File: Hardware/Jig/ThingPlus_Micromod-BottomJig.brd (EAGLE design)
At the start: 124.5 x 97.8 mm, 116 parts, among them J4 USB_A_PTH_MALE, J5 USB_A_SMT_FEMALE, U2 74LVC4066, U3 74LVC4066, U5 74LVC4066_MUX_1:1_X4

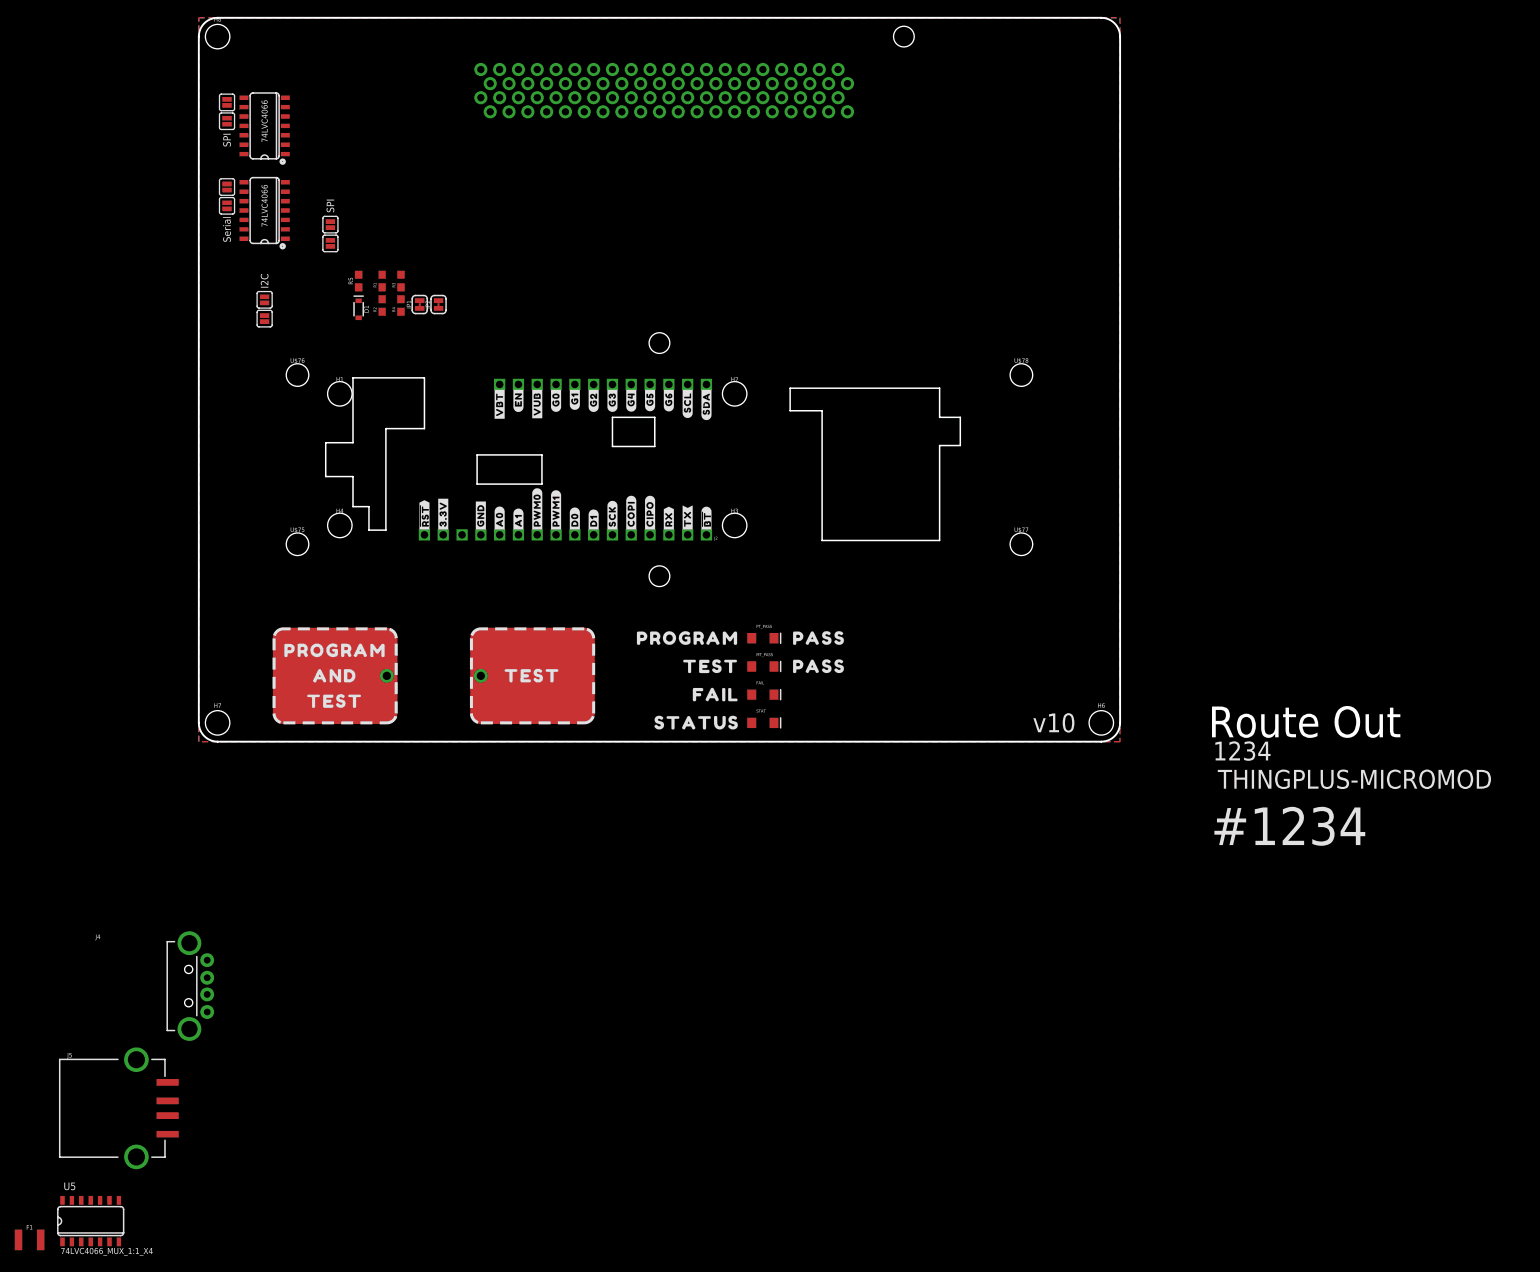
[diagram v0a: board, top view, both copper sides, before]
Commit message: Preliminary version of test jig bottom board uploaded
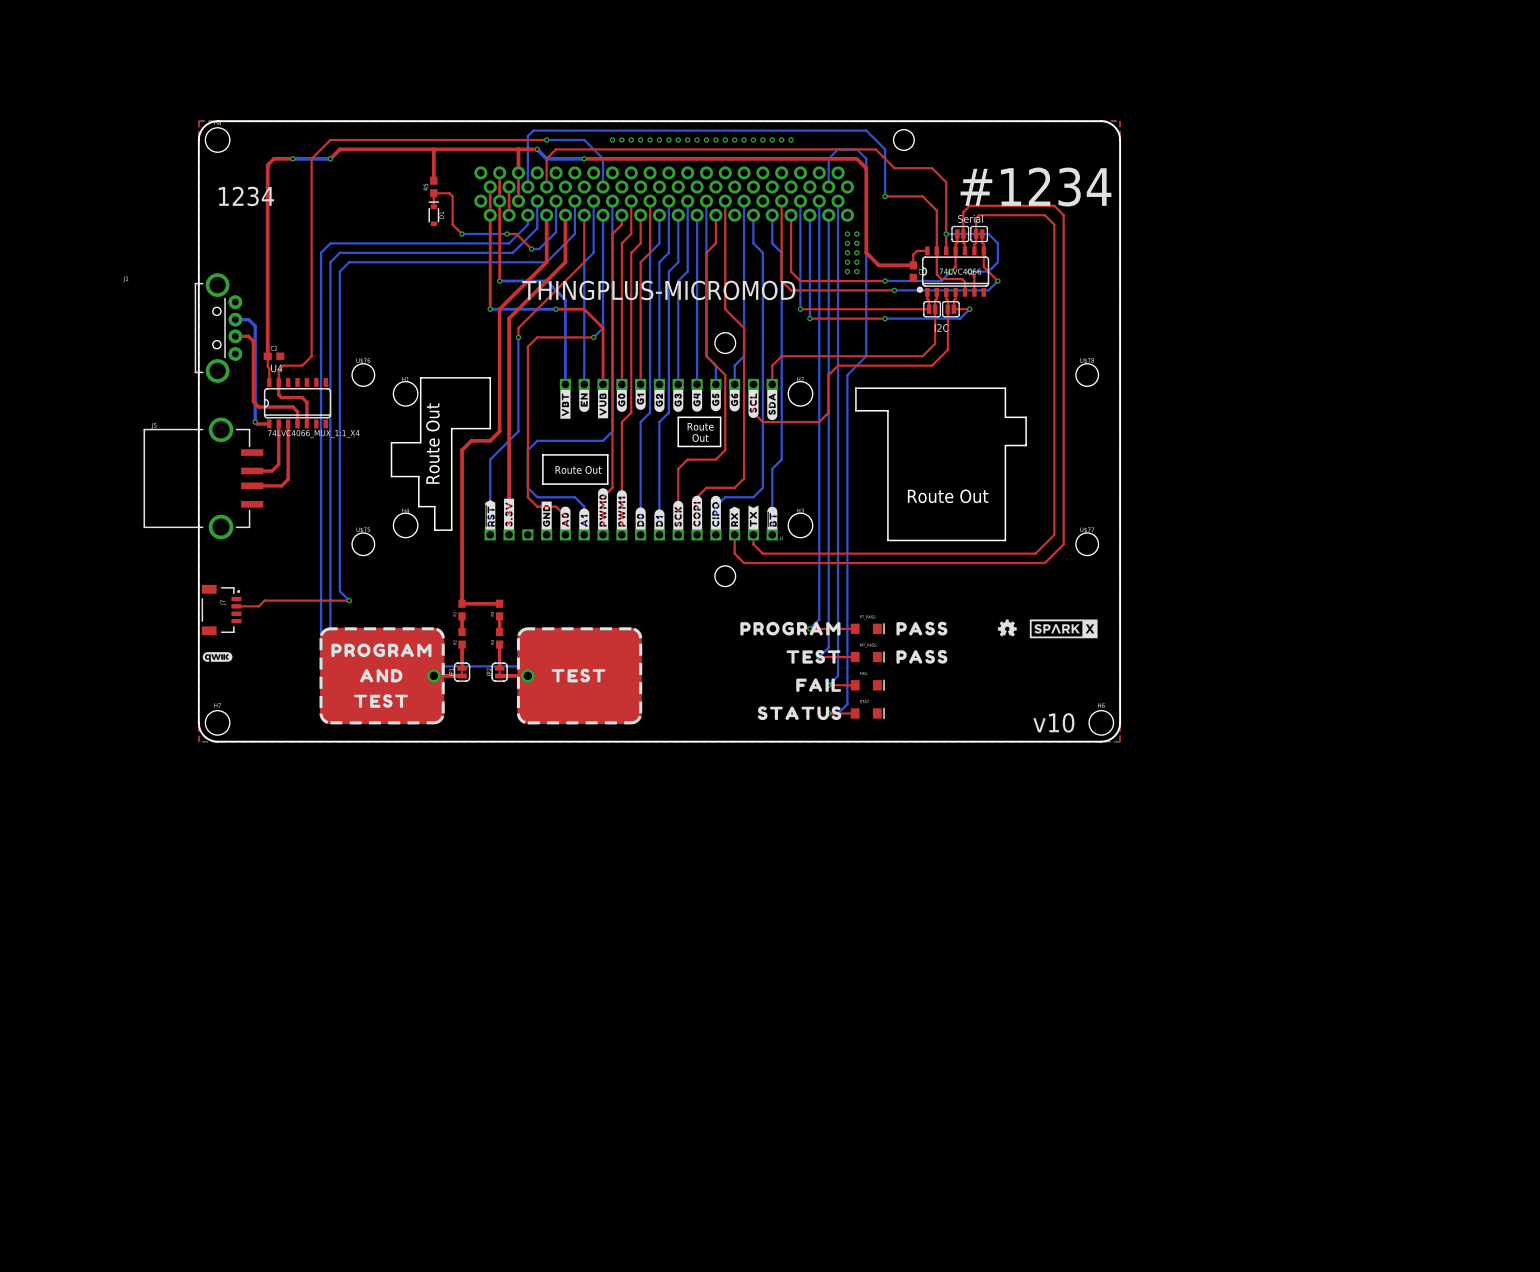
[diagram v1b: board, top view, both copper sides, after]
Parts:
- removed F1: 6V/2A, SparkFun-Fuses:1210
- removed J4: USB_A_PTH_MALE, SparkFun-Connectors:USB-A-H
- removed J_SCL3, J_SCL4, J_SCL5, J_SDA1: JUMPER-SMT_2_NO_SILK, SparkFun-Jumpers:SMT-JUMPER_2_NO_SILK
- removed U$41: (no value), output:#VE#16
- removed U$66: (no value), output:#MEAS#25
- removed U$69: (no value), output:#3#3V_LED#25
- removed U$70: (no value), output:#VIN_LED#25
- removed U$72: (no value), output:#I2C#27
- removed U$73: (no value), output:THINGPLUS_MICROMOD29
- removed U$74: (no value), output:#SCL#G7#27
- removed U$81: TB_MAIN_BRAIN_CARDEDGE_TB_SIDE, Testing:TB_CARDEDGE
- removed U3: 74LVC4066, SparkFun-IC-Logic:SO14
- removed U5: 74LVC4066_MUX_1:1_X4, Testing:SO14
- added C1, C2: 0.1uF, SparkFun-Capacitors:0603
- added J1: USB_A_PTH_MALE, SparkFun-Connectors:USB-A-H
- added J7: QWIIC_RIGHT_ANGLE, SparkFun-Connectors:JST04_1MM_RA
- added LOGO2: OSHW-LOGOMINI, SparkFun-Aesthetics:OSHW-LOGO-MINI
- added LOGO4: QWIIC_LOGO_4MM, SparkFun-Aesthetics:QWIIC_4MM
- added U$1: SPARKX-LOGO4, SparkX:SPARKX-MEDIUM
- added U1: TB_MAIN_BRAIN_CARDEDGE_TB_SIDE, Testing:TB_CARDEDGE
- added U4: 74LVC4066_MUX_1:1_X4, Testing:SO14
- moved J_SCL1 101.8 mm to (114.3, 74.9), turned to 180 degrees
- moved J_SDA 99.1 mm to (111.8, 74.9), turned to 0 degrees
- moved U2 93.0 mm to (110.5, 69.8), turned to 0 degrees
- moved J_SCL 92.7 mm to (110.5, 64.8), turned to 180 degrees
- moved J_SCL2 90.2 mm to (108.0, 64.8), turned to 0 degrees
- moved J5 85.9 mm to (8.89, 41.9)
- moved JP2 50.3 mm to (49.5, 15.7)
- moved JP1 50.0 mm to (44.5, 15.7)
- moved R4 46.9 mm to (49.5, 20.3)
- moved R3 46.4 mm to (49.5, 24.1)
- moved R2 46.2 mm to (44.5, 20.3)
- moved R1 45.7 mm to (44.5, 24.1)
- moved FRAME2 44.1 mm to (53.3, -8.89)
- moved D1 16.3 mm to (40.6, 77.5)
- moved R5 16.3 mm to (40.6, 81.3)
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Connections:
- removed net !BOOT!: J2.1
- removed net !RST!: J2.16
- removed net 3.3V: J2.15
- removed net A0: J2.12
- removed net A1: J2.11
- removed net D0: J2.8
- removed net D1: J2.7
- removed net EN: J3.11
- removed net G0: J3.9
- removed net G1: J3.8
- removed net G2: J3.7
- removed net G3: J3.6
- removed net G4: J3.5
- removed net G5: J3.4
- removed net G6: J3.3
- removed net J_10: U$81.P38
- removed net J_11: U$81.P34
- removed net J_12: U$81.P30
- removed net J_13: U$81.P26
- removed net J_14: U$81.P23
- removed net J_15: U$81.P21
- removed net J_16: U$81.P19
- removed net J_17: U$81.P17
- removed net J_2: U$81.P37
- removed net J_27: U$81.P50
- removed net J_28: U$81.P46
- removed net J_29: U$81.P42
- removed net J_3: U$81.P35
- removed net J_5: U$81.P33
- removed net J_6: U$81.P31
- removed net J_7: U$81.P29
- removed net J_8: U$81.P27
- removed net J_9: U$81.P25
- removed net J_A1: U$81.P61
- removed net J_A10: U$81.P43
- removed net J_A11: U$81.P41
- removed net J_A12: U$81.P39
- removed net J_A2: U$81.P59
- removed net J_A3: U$81.P57
- removed net J_A4: U$81.P55
- removed net J_A5: U$81.P53
- removed net J_A6: U$81.P51
- removed net J_A7: U$81.P49
- removed net J_A8: U$81.P47
- removed net J_A9: U$81.P45
- removed net PWM0: J2.10
- removed net PWM1: J2.9
- removed net SCL/G7: J3.2
- removed net SDA: J3.1
- removed net SPI_CIPO: J2.4
- removed net SPI_COPI: J2.5
- removed net SPI_SCK: J2.6
- removed net TARGET_CIPO: J_SCL5.2, U3.2
- removed net TARGET_COPI: J_SCL3.2, U3.3
- removed net TARGET_CS: J_SDA1.2, U3.10
- removed net TARGET_RX: J_SCL1.2, U2.9
- removed net TARGET_SCK: J_SCL4.2, U3.9
- removed net TARGET_SCL: J_SCL.2, U2.3
- removed net TARGET_SDA: J_SCL2.2, U2.2
- removed net TARGET_TX: J_SDA.2, U2.10
- removed net UART_RX: J2.3
- removed net UART_TX: J2.2
- removed net V_BATT: J3.12
- removed net V_USB: J3.10
- new net !MICROMOD_BOOT!: J2.1, U1.P17
- new net !MICROMOD_RST!: J2.16, U1.P57
- new net BRD_USB_D+: J5.D-, U4.2
- new net BRD_USB_D-: J5.D+, U4.3
- new net J_19: U1.P19
- new net J_30: U1.P30
- new net J_34: U1.P34
- new net J_38: U1.P38
- new net J_42: U1.P42
- new net J_46: U1.P46
- new net J_50: U1.P50
- new net J_58: U1.P58
- new net MICROMOD_3V3: J2.15, U1.P61
- new net MICROMOD_A0: J2.12, U1.P53
- new net MICROMOD_A1: J2.11, U1.P51
- new net MICROMOD_CIPO: J2.4, U1.P21
- new net MICROMOD_COPI: J2.5, U1.P27
- new net MICROMOD_D0: J2.8, U1.P41
- new net MICROMOD_D1: J2.7, U1.P37
- new net MICROMOD_EN: J3.11, U1.P55
- new net MICROMOD_G0: J3.9, U1.P47
- new net MICROMOD_G1: J3.8, U1.P43
- new net MICROMOD_G2: J3.7, U1.P39
- new net MICROMOD_G3: J3.6, U1.P35
- new net MICROMOD_G4: J3.5, U1.P33
- new net MICROMOD_G5: J3.4, U1.P31
- new net MICROMOD_G6: J3.3, U1.P23
- new net MICROMOD_PWM0: J2.10, U1.P49
- new net MICROMOD_PWM1: J2.9, U1.P45
- new net MICROMOD_QWIIC_PWR: J7.2, U1.P59
- new net MICROMOD_RX: J2.2, J_SCL1.2, U2.9
- new net MICROMOD_SCK: J2.6, U1.P29
- new net MICROMOD_SCL: J3.2, J_SCL.2, U2.3
- new net MICROMOD_SDA: J3.1, J_SCL2.2, U2.2
- new net MICROMOD_TX: J2.3, J_SDA.2, U2.10
- new net NC: J5.VBUS
- new net USB_D+: J1.D+, U4.1
- new net USB_D-: J1.D-, U4.4
- new net USB_SWCH_EN: U1.P54, U4.13, U4.5
- net BRAIN_VCC: now also C1.1, C2.1, U1.P71, U1.P72, U4.14; no longer U$81.P71, U$81.P72, U3.14
- net BRAIN_VCC_A0: now also U1.P63; no longer U$81.P63
- net FAILURE_LED: now also U1.P3; no longer U$81.P3
- net GND: now also C1.2, C2.2, J1.GND, J7.1, U1.P1, U1.P2, U1.P79, U1.P80, U4.12, U4.6, U4.7; no longer J4.GND, U$81.P1, U$81.P2, U$81.P79, U$81.P80, U3.7
- net J_25: now also U1.P25; no longer U$81.P58
- net J_26: now also U1.P26; no longer U$81.P54
- net J_CIPO: now also U1.P14; no longer J_SCL5.1, U$81.P14, U3.1
- net J_COPI: now also U1.P10; no longer J_SCL3.1, U$81.P10, U3.4
- net J_CS: now also U1.P4; no longer J_SDA1.1, U$81.P4, U3.11
- net J_I2C_EN: now also U1.P70; no longer U$81.P70
- net J_MICROSD_!CS!: now also U1.P18; no longer U$81.P18
- net J_MICROSD_EN: now also U1.P22; no longer U$81.P22
- net J_MICROSD_PWR_EN: now also U1.P12; no longer U$81.P12
- net J_RX1-I: now also U1.P13; no longer U$81.P13
- net J_SCK: now also U1.P8; no longer J_SCL4.1, U$81.P8, U3.8
- net J_SCL: now also U1.P9; no longer U$81.P9
- net J_SDA: now also U1.P11; no longer U$81.P11
- net J_SERIAL_EN: now also U1.P66; no longer U$81.P66
- net J_SPI_EN: now also U1.P62; no longer U$81.P62, U3.12, U3.13, U3.5, U3.6
- net J_TX1-O: now also U1.P15; no longer U$81.P15
- net MT_PASS_LED: now also U1.P5; no longer U$81.P5
- net N$1: now also U1.P65; no longer U$81.P65
- net N$15: now also U1.P69; no longer U$81.P69
- net N$18: now also U1.P67; no longer U$81.P67
- net PT_PASS_LED: now also U1.P7; no longer U$81.P7
- net RAW: now also U1.P73, U1.P74; no longer U$81.P73, U$81.P74
- net STAT_LED: now also U1.P6; no longer U$81.P6
- net V1: now also J3.10, U1.P77, U1.P78; no longer U$81.P77, U$81.P78
- net V2: now also J3.12, U1.P75, U1.P76; no longer U$81.P75, U$81.P76
- net VBUS: now also J1.VBUS; no longer J4.VBUS, J5.VBUS
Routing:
- net BRAIN_VCC: track 0.00 -> 145.5 mm, vias 0 -> 4
- net N$18: track 0.00 -> 118.4 mm
- net MICROMOD_TX: track 0.00 -> 112.8 mm
- net N$15: track 0.00 -> 106.2 mm
- net MICROMOD_RX: track 0.00 -> 101.2 mm
- net MICROMOD_QWIIC_PWR: track 0.00 -> 98.8 mm, vias 0 -> 1
- net STAT_LED: track 0.00 -> 91.3 mm, vias 0 -> 1
- net USB_SWCH_EN: track 0.00 -> 87.6 mm, vias 0 -> 1
- net J_SERIAL_EN: track 0.00 -> 86.9 mm, vias 0 -> 2
- net J_I2C_EN: track 0.00 -> 84.9 mm, vias 0 -> 1
- net FAILURE_LED: track 0.00 -> 69.5 mm, vias 0 -> 1
- net MT_PASS_LED: track 0.00 -> 65.1 mm, vias 0 -> 1
- net PT_PASS_LED: track 0.00 -> 64.4 mm, vias 0 -> 1
- net N$1: track 0.00 -> 63.8 mm
- net MICROMOD_A1: track 0.00 -> 61.2 mm
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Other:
- board size 124.5 x 97.8 mm -> 124.5 x 83.8 mm
- board text removed: "SPI"
